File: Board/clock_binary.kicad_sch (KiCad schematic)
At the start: 40 parts, among them U3 4081, U6 4040, U7 4040, U8 4040, U9 4082

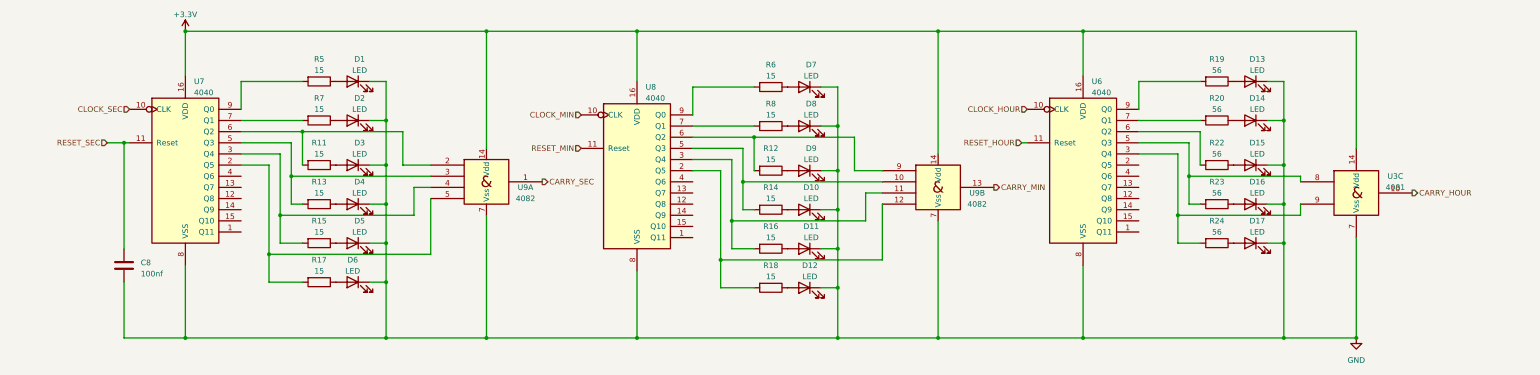
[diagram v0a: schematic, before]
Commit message: add caps to all resets
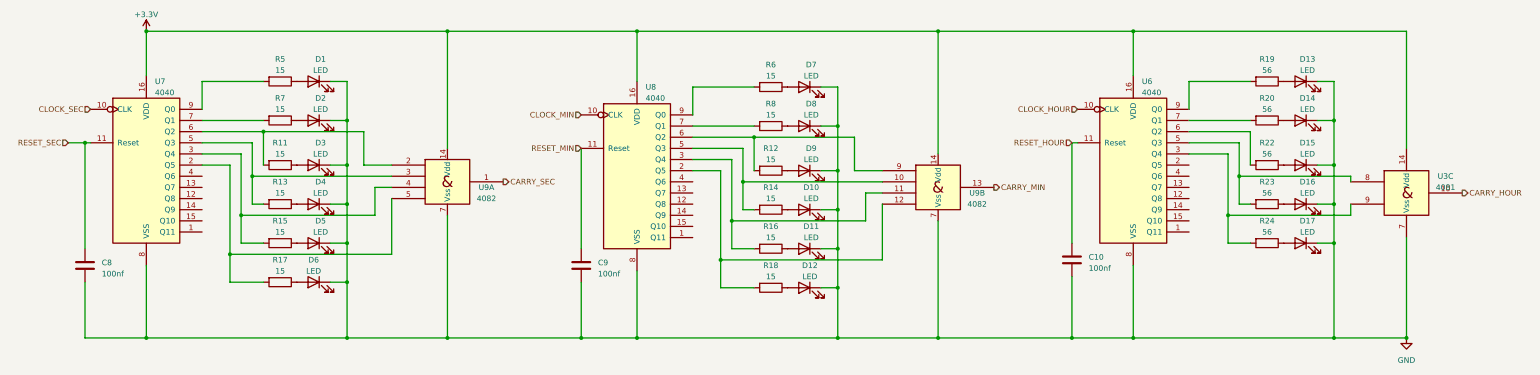
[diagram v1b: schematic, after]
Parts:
- added C10, C9: 100nf, Capacitor_THT:C_Disc_D5.1mm_W3.2mm_P5.00mm, symbol Device:C
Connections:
- net GND: now also C10.2, C9.2
- net RESET_HOUR: now also C10.1
- net RESET_MIN: now also C9.1
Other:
- moved on the sheet: C8, D1, D13, D14, D15, D16, D17, D2, D3, D4, D5, D6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
